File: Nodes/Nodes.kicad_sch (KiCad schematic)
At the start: 31 parts, among them J1 Conn_01x04_Socket, J2 Barrel_Jack_MountingPin, J3 Screw_Terminal_01x03, J4 Screw_Terminal_01x03, SW1 SW_Push, U1 NRF24L01_Breakout, U2 NRF24L01_Breakout, U3 AMS1117-3.3, U4 YAAJ_BluePill_Part_Like, U5 NRF24L01_Breakout

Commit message: chore: add labels to switch
rename OLED port on pcb to I2C, added "TRAIN DIR" text to switch on schematic and PCB.
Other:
- note added: "SIGNAL RESET/ TRAIN DIR"
- note removed: "SIGNAL RESET"
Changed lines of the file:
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@@
 		)
 	)
-	(text "SIGNAL RESET\n"
+	(text "SIGNAL RESET/ TRAIN DIR\n"
 		(exclude_from_sim no)
-		(at 37.084 52.07 0)
+		(at 42.926 52.324 0)
 		(effects
 			(font

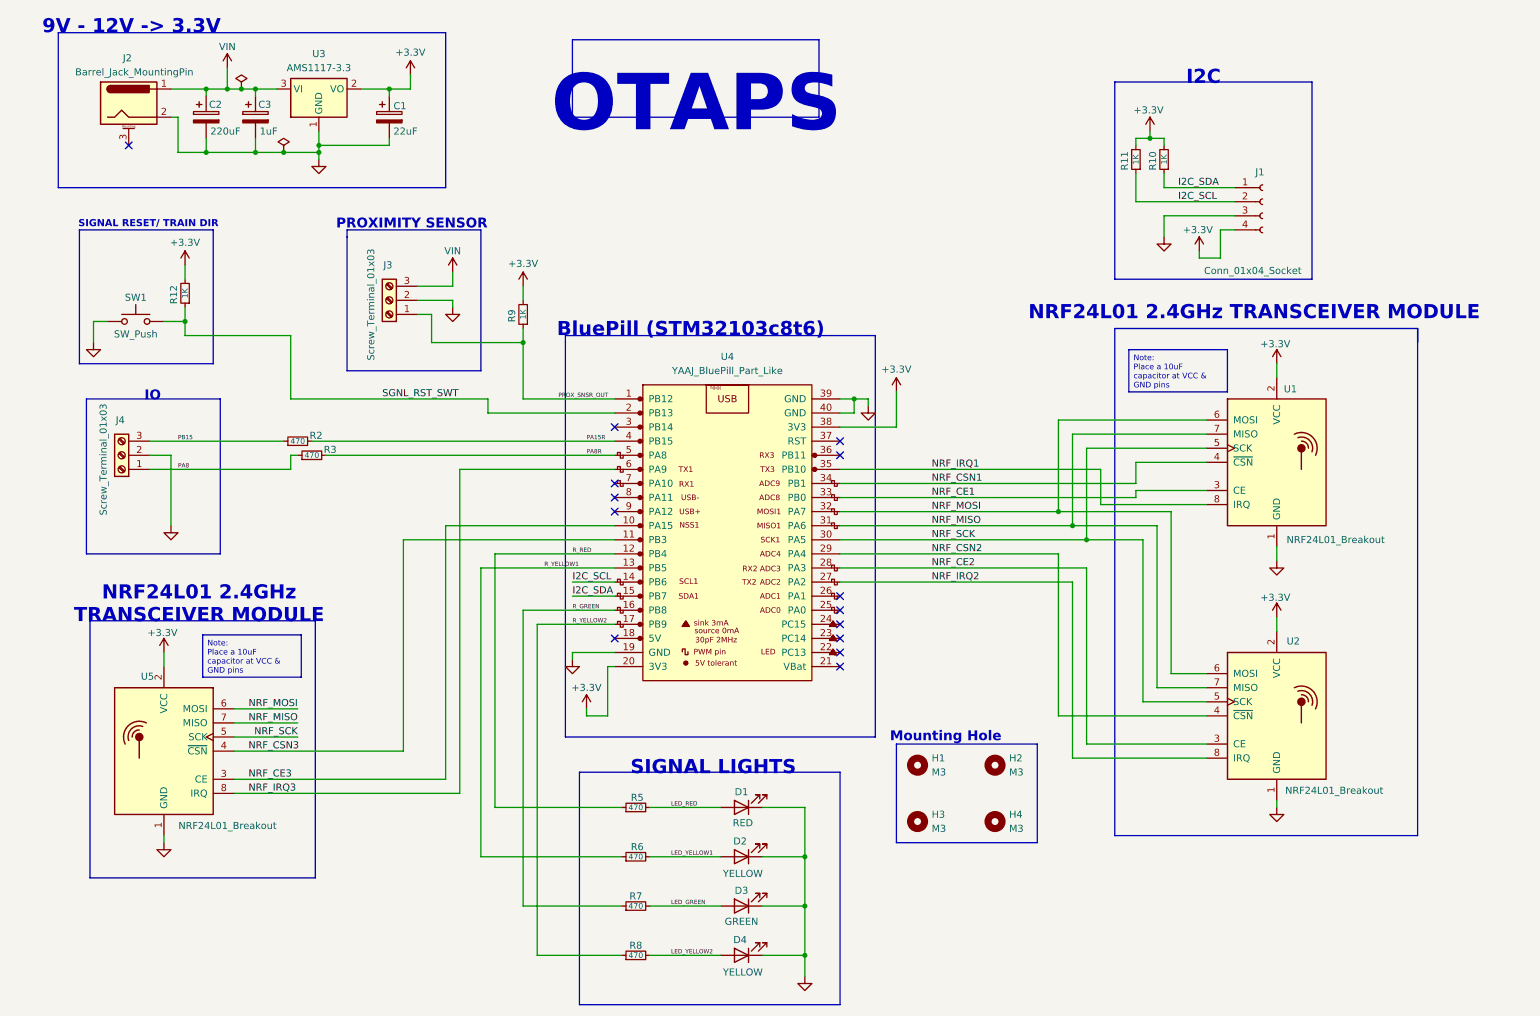
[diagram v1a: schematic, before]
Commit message: chore: change connections for NRF24(U5), IO port and LEDs
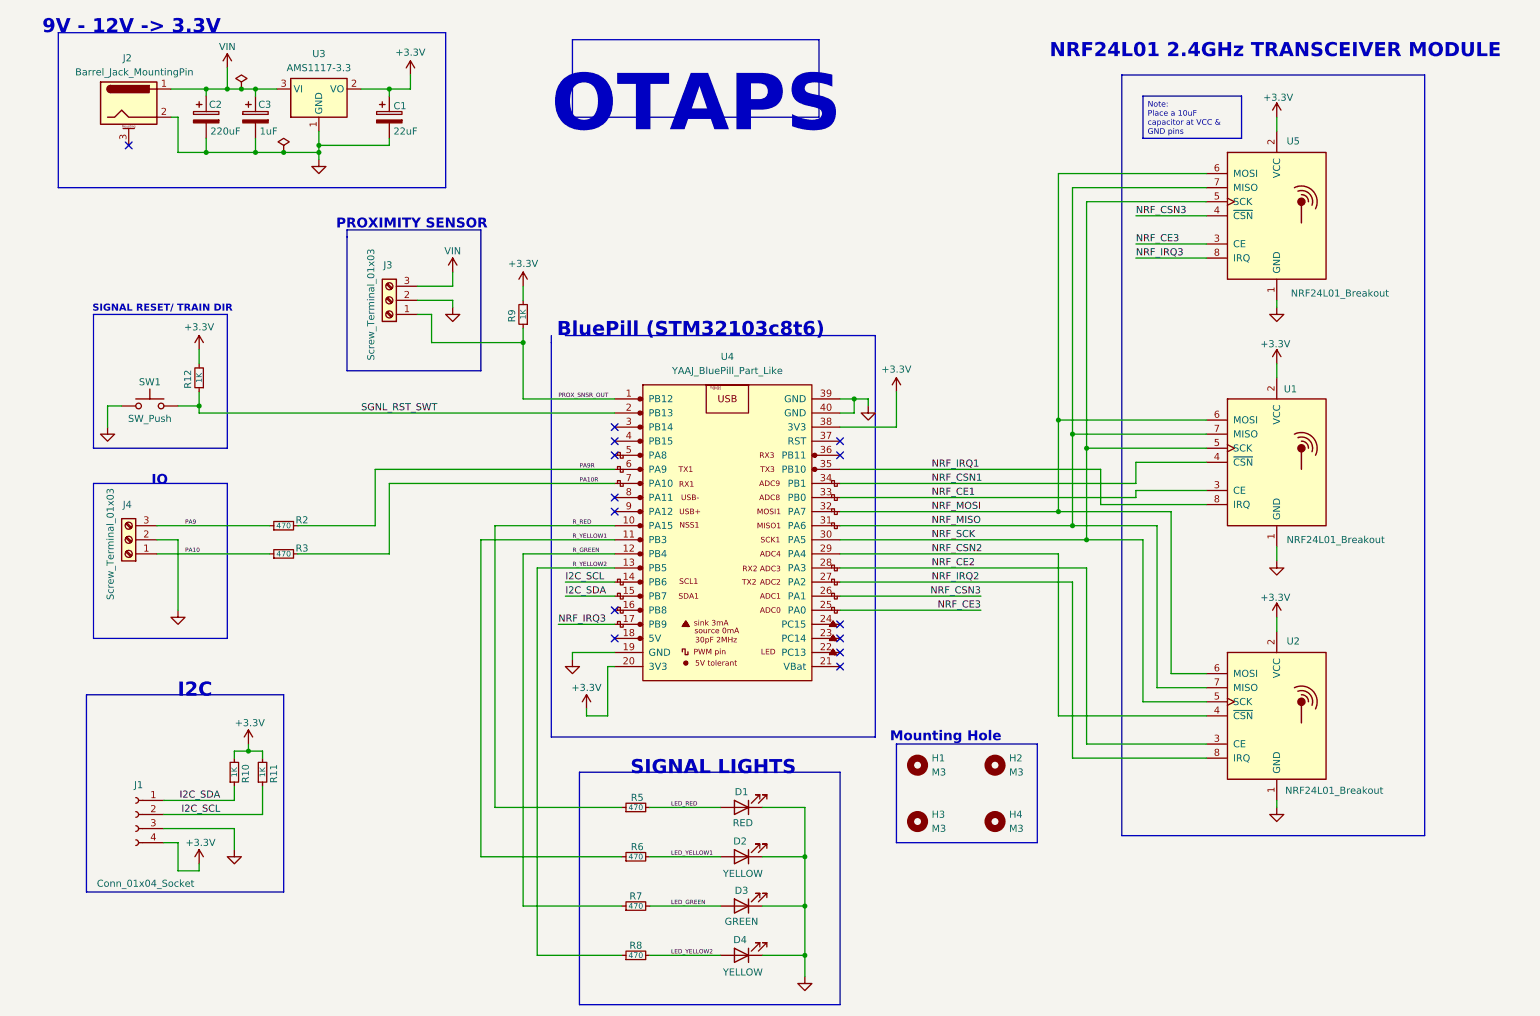
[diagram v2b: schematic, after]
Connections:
- net NRF_CE3: now also U4.25 (PA0); no longer U4.10 (PA15)
- net NRF_CSN3: now also U4.26 (PA1); no longer U4.11 (PB3)
- net NRF_IRQ3: now also U4.17 (PB9); no longer U4.6 (PA9)
- net R_GREEN: now also U4.12 (PB4); no longer U4.16 (PB8)
- net R_RED: now also U4.10 (PA15); no longer U4.12 (PB4)
- net R_YELLOW1: now also U4.11 (PB3); no longer U4.13 (PB5)
- net R_YELLOW2: now also U4.13 (PB5); no longer U4.17 (PB9)
- net PA10R: now reaches U4.7 (PA10)
- net PA10R: now also R3.2
- net PA15R: no longer names the net of U4.4 (PB15)
- net PA15R: no longer R2.2
- net PA8 renamed PA10
- net PA8R: no longer names the net of U4.5 (PA8)
- net PA8R: no longer R3.2
- net PB15 renamed PA9
- new net PA9R: R2.2, U4.6 (PA9)
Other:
- moved on the sheet: J1, J4, R10, R11, R12, R2, R3, SW1, U5

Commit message: fix: change silkscreen line width to 0.152 and update vendor link for resistors and NRF24
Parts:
- R10, R11, R12, R9: Vendor Link https://robu.in/product/330-ohm-1-4w-0603-surface-mount-chi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 -> https://robu.in/product/rc0805fr-071kl-yageo-res-thick-film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
- R2, R3, R5, R6, R7, R8: Vendor Link https://robu.in/product/330-ohm-1-4w-0603-surface-mount-chi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 -> https://robu.in/product/ac0805fr-7w470rl-yageo-res-thick-fi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
- SW1: Vendor Link (none) -> https://robu.in/product/tact-switch-tk-066-4-pins-6x6-smd/
- U1, U2, U5: Vendor Link (none) -> https://robu.in/product/m177-nrf24l01-2-4ghz-antenna-wirele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
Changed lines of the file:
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@@
 	(polyline
 		(pts
-			(xy 173.99 72.39) (xy 118.11 72.39)
+			(xy 173.99 72.39) (xy 115.57 72.39)
 		)
 		(stroke
@@
 			)
 		)
-		(property "Vendor Link" "https://robu.in/product/330-ohm-1-4w-0603-surface-mount-chip-resistor-pack-of-100/"
+		(property "Vendor Link" "https://robu.in/product/ac0805fr-7w470rl-yageo-res-thick-film-0805-470-ohm-1-0-25w1-4w-%c2%b1100ppm-c-pad-smd-t-r-automotive-aec-q200/"
 			(at 130.81 166.37 0)
 			(effects
@@
 			)
 		)
-		(property "Vendor Link" "https://robu.in/product/330-ohm-1-4w-0603-surface-mount-chip-resistor-pack-of-100/"
+		(property "Vendor Link" "https://robu.in/product/rc0805fr-071kl-yageo-res-thick-film-0805-1k-ohm-1-0-125w1-8w-%c2%b1100ppm-c-pad-smd-t-r/"
 			(at 58.42 151.13 0)
 			(effects
@@
 			)
 		)
-		(property "Vendor Link" "https://robu.in/product/330-ohm-1-4w-0603-surface-mount-chip-resistor-pack-of-100/"
+		(property "Vendor Link" "https://robu.in/product/ac0805fr-7w470rl-yageo-res-thick-film-0805-470-ohm-1-0-25w1-4w-%c2%b1100ppm-c-pad-smd-t-r-automotive-aec-q200/"
 			(at 130.81 175.26 0)
 			(effects
@@
 			)
 		)
-		(property "Vendor Link" "https://robu.in/product/330-ohm-1-4w-0603-surface-mount-chip-resistor-pack-of-100/"
+		(property "Vendor Link" "https://robu.in/product/ac0805fr-7w470rl-yageo-res-thick-film-0805-470-ohm-1-0-25w1-4w-%c2%b1100ppm-c-pad-smd-t-r-automotive-aec-q200/"
 			(at 130.81 184.15 0)
 			(effects
@@
 			)
 		)
+		(property "Vendor Link" "https://robu.in/product/m177-nrf24l01-2-4ghz-antenna-wireless-transceiver-module/"
+			(at 246.38 95.25 0)
+			(effects
+				(font
+					(size 1.27 1.27)
+				)
+				(hide yes)
+			)
+		)
 		(pin "1"
 		)
@@
 			)
 		)
-		(property "Vendor Link" "https://robu.in/product/330-ohm-1-4w-0603-surface-mount-chip-resistor-pack-of-100/"
+		(property "Vendor Link" "https://robu.in/product/rc0805fr-071kl-yageo-res-thick-film-0805-1k-ohm-1-0-125w1-8w-%c2%b1100ppm-c-pad-smd-t-r/"
 			(at 63.5 151.13 0)
 			(effects
@@
 			)
 		)
-		(property "Vendor Link" "https://robu.in/product/330-ohm-1-4w-0603-surface-mount-chip-resistor-pack-of-100/"
+		(property "Vendor Link" "https://robu.in/product/ac0805fr-7w470rl-yageo-res-thick-film-0805-470-ohm-1-0-25w1-4w-%c2%b1100ppm-c-pad-smd-t-r-automotive-aec-q200/"
 			(at 130.81 157.48 0)
 			(effects
@@
 			)
 		)
-		(property "Vendor Link" "https://robu.in/product/330-ohm-1-4w-0603-surface-mount-chip-resistor-pack-of-100/"
+		(property "Vendor Link" "https://robu.in/product/ac0805fr-7w470rl-yageo-res-thick-film-0805-470-ohm-1-0-25w1-4w-%c2%b1100ppm-c-pad-smd-t-r-automotive-aec-q200/"
 			(at 67.31 106.68 0)
 			(effects
@@
 			)
 		)
+		(property "Vendor Link" "https://robu.in/product/m177-nrf24l01-2-4ghz-antenna-wireless-transceiver-module/"
+			(at 246.38 140.97 0)
+			(effects
+				(font
+					(size 1.27 1.27)
+				)
+				(hide yes)
+			)
+		)
 		(pin "1"
 		)
@@
 			)
 		)
-		(property "Vendor Link" "https://robu.in/product/330-ohm-1-4w-0603-surface-mount-chip-resistor-pack-of-100/"
+		(property "Vendor Link" "https://robu.in/product/rc0805fr-071kl-yageo-res-thick-film-0805-1k-ohm-1-0-125w1-8w-%c2%b1100ppm-c-pad-smd-t-r/"
 			(at 52.07 80.01 0)
 			(effects
@@
 			)
 		)
+		(property "Vendor Link" "https://robu.in/product/tact-switch-tk-066-4-pins-6x6-smd/"
+			(at 43.18 85.09 0)
+			(effects
+				(font
+					(size 1.27 1.27)
+				)
+				(hide yes)
+			)
+		)
 		(pin "1"
 		)
@@
 			)
 		)
-		(property "Vendor Link" "https://robu.in/product/330-ohm-1-4w-0603-surface-mount-chip-resistor-pack-of-100/"
+		(property "Vendor Link" "https://robu.in/product/ac0805fr-7w470rl-yageo-res-thick-film-0805-470-ohm-1-0-25w1-4w-%c2%b1100ppm-c-pad-smd-t-r-automotive-aec-q200/"
 			(at 67.31 111.76 0)
 			(effects
@@
 			)
 		)
-		(property "Vendor Link" "https://robu.in/product/330-ohm-1-4w-0603-surface-mount-chip-resistor-pack-of-100/"
+		(property "Vendor Link" "https://robu.in/product/rc0805fr-071kl-yageo-res-thick-film-0805-1k-ohm-1-0-125w1-8w-%c2%b1100ppm-c-pad-smd-t-r/"
 			(at 110.49 68.58 0)
 			(effects
@@
 			(at 246.38 50.8 0)
 			(effects
+				(font
+					(size 1.27 1.27)
+				)
+				(hide yes)
+			)
+		)
+		(property "Vendor Link" "https://robu.in/product/m177-nrf24l01-2-4ghz-antenna-wireless-transceiver-module/"
+			(at 246.38 50.8 0)
+			(effects
